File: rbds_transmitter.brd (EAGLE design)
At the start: 80 x 75.9 mm, 136 parts, among them J2 AVRISP-6, Q1 P-CH, Q2 P-Ch, Q3 P-Ch, T1 ATB3225-75032CT, T2 ATB3225-75032CT, U1 MAX2606, U2 TS974, U3 TS974, U4 MAX1551, U5 ATMEGA328, U6 TPS61030, U7 MCP4812, X1 16Mhz

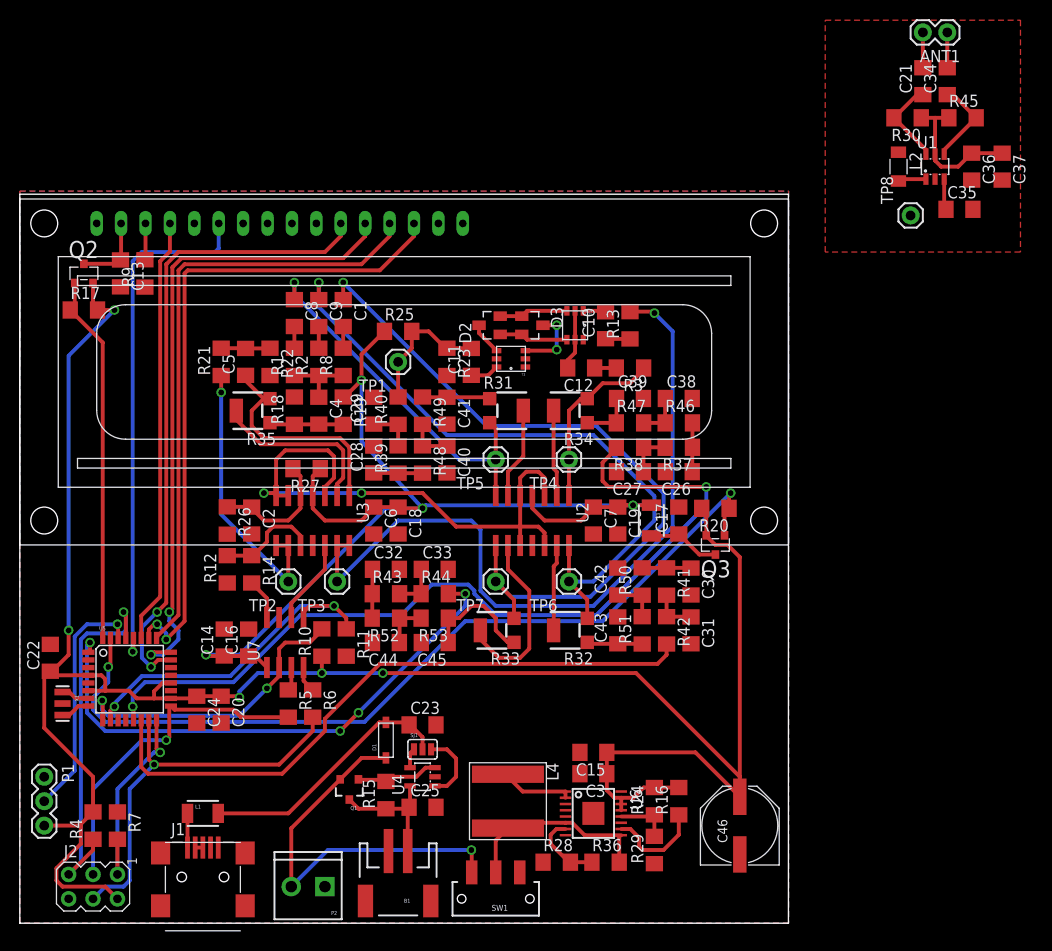
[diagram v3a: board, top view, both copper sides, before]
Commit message: renubmered everything, request engineering change forum
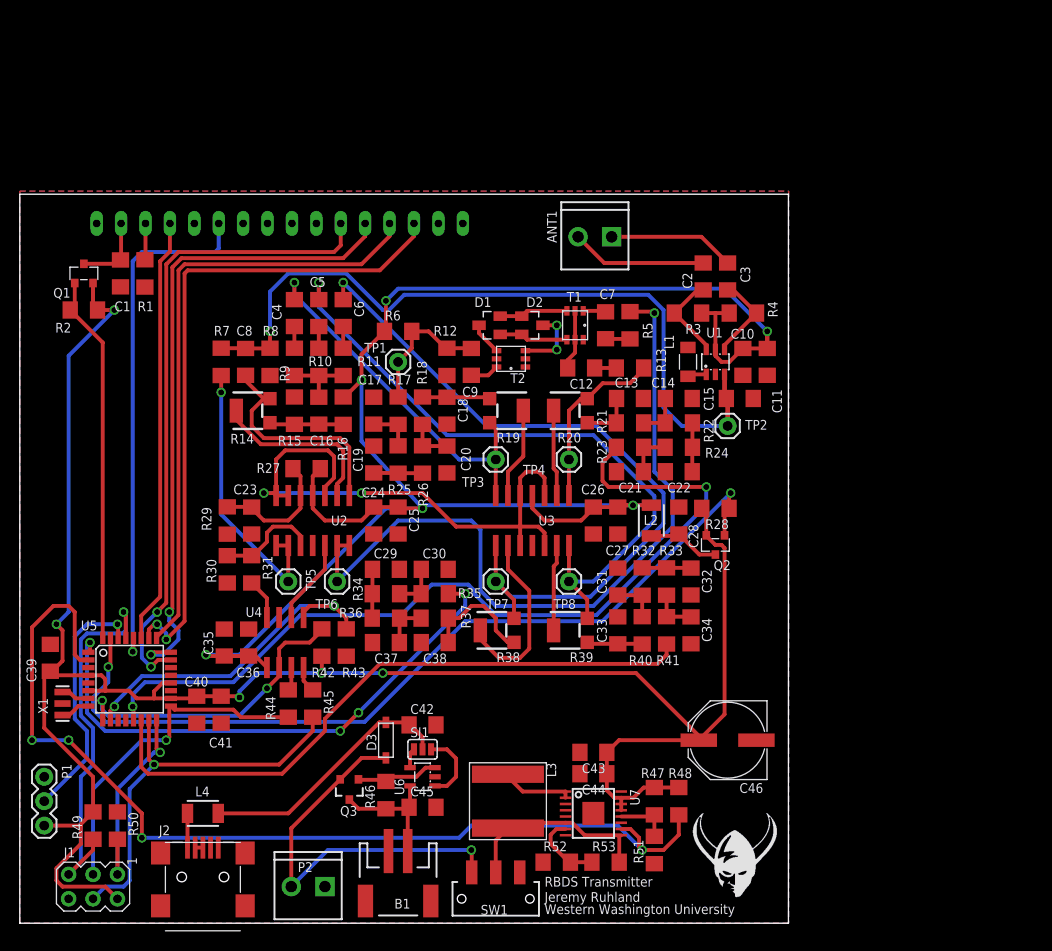
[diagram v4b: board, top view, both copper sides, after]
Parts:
- ANT1: value (none) -> 2.5MM; device dipole_antenna:ANT -> dipole_antenna:2.5MM_SCREW
- C1: value 1uF -> 4.7uF
- C10: value 10uF -> 1uF
- C11: value 10uF -> 4.7uF
- C13, C14: value 4.7uF -> 1.5nF
- C15: value 4.7uF -> 1nF
- C16, C24: value 0.1uF -> 1uF
- C17, C18, C19, C20: value 4.7uF -> 1.2nF
- C2, C3: value 1uF -> 1nF
- C21: value 1nF -> 1.5nF
- C22: value 0.1uF -> 1.5nF
- C23: value 4.7uF -> 1uF
- C26: value 1.5nF -> 1uF
- C27: value 1.5nF -> 4.7uF
- C28, C41: value 1.2nF -> 4.7uF
- C29: value 1.2nF -> 3nF
- C30: value 3.9nF -> 3nF
- C32, C33: value 3nF -> 3.9nF
- C34: value 1nF -> 3.9nF
- C35: value 1nF -> 4.7uF
- C36: value 1uF -> 0.1uF
- C37: value 4.7uF -> 3nF
- C38: value 1.5nF -> 3nF
- C39: value 1.5nF -> 0.1uF
- C40: value 1.2nF -> 0.1uF
- C42, C43: value 3.9nF -> 4.7uF
- C44: value 3nF -> 1uF
- C45: value 3nF -> 4.7uF
- C7, C9: value 1uF -> 10uF
- D1: value (none) -> BAS40-04; device adafruit:SOD-123 -> diode:SOT23
- D3: value BAS40-04 -> (none); device diode:SOT23 -> adafruit:SOD-123
- J1: value (none) -> AVRISP-6; device adafruit:USB-MINIB -> adafruit:AVRISP
- J2: value AVRISP-6 -> (none); device adafruit:AVRISP -> adafruit:USB-MINIB
- L1: value (none) -> 485nH; device sparkfun:1210 -> resistor:L3216C
- L2: value 485nH -> 10mH; device resistor:L3216C -> sparkfun:1210
- L3: value 10mH -> 6.8uH; device sparkfun:1210 -> yuden:8040
- L4: value 6.8uH -> (none); device yuden:8040 -> sparkfun:1210
- LCD1: value HD44780LCD-1602 -> HD44780LCDNOSILK; device adafruit:LCD1602 -> adafruit:LCD1602_NOSILK
- Q1: value P-CH -> P-Ch; device sparkfun:SOT23-3 -> transistor-power:MICRO3
- Q3: value P-Ch -> P-CH; device transistor-power:MICRO3 -> sparkfun:SOT23-3
- R1: value 1k -> 332
- R10, R11: value 10k -> 1k
- R12, R6, R7: value 10k -> 100k
- R14: value 10k -> 100k; device adafruit:R1206 -> rcl:RTRIM3304W
- R17, R18, R21, R22, R23, R25, R26: value 100k -> 2k
- R19, R20: device adafruit:R1206 -> rcl:RTRIM3304W
- R2, R8: value 1k -> 100k
- R24: value 1.8M -> 2k
- R28: value 390k -> 100k
- R29: value 200k -> 100k
- R3: value 200 -> 100
- R30, R45: value 100 -> 10k
- R31: value 100k -> 10k; device rcl:RTRIM3304W -> adafruit:R1206
- R32, R33, R34, R35: value 100k -> 2k; device rcl:RTRIM3304W -> adafruit:R1206
- R36: value 1.95M -> 2k
- R38, R39: value 2k -> 100k; device adafruit:R1206 -> rcl:RTRIM3304W
- R4: value 10k -> 100
- R42, R43, R44, R49, R50: value 2k -> 10k
- R46, R48: value 2k -> 100k
- R47: value 2k -> 1.8M
- R5: value 10k -> 200
- R51: value 2k -> 200k
- R52: value 2k -> 390k
- R53: value 2k -> 1.95M
- R9: value 332 -> 1k
- U4: value MAX1551 -> MCP4812; device maxim:SOT23-5L -> microchip:SO-08
- U6: value TPS61030 -> MAX1551; device texas:HTSSOP16 -> maxim:SOT23-5L
- U7: value MCP4812 -> TPS61030; device microchip:SO-08 -> texas:HTSSOP16
- moved R45 91.0 mm to (30.5, 22.9), turned to 270 degrees
- moved C36 90.1 mm to (23.8, 29.2), turned to 90 degrees
- moved C35 88.8 mm to (21.3, 29.2), turned to 90 degrees
- moved R4 86.1 mm to (75.2, 63.5), turned to 0 degrees
- moved R30 85.0 mm to (21.6, 36.8), turned to 90 degrees
- moved C37 81.0 mm to (38.1, 29.2), turned to 180 degrees
- moved Q2 71.5 mm to (72.4, 39.4), turned to 180 degrees
- moved L1 69.0 mm to (69.5, 58.4), turned to 270 degrees
- moved C22 68.2 mm to (68.6, 47.0), turned to 180 degrees
- moved C39 66.1 mm to (3.17, 27.6), turned to 90 degrees
- moved C34 63.1 mm to (69.8, 30.5), turned to 270 degrees
- moved Q1 60.4 mm to (6.67, 67.6), turned to 0 degrees
- moved R50 60.2 mm to (10.2, 10.2), turned to 270 degrees
- moved R29 56.1 mm to (21.6, 41.9), turned to 270 degrees
- moved R49 55.1 mm to (7.62, 10.2), turned to 90 degrees
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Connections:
- net !DAC_CS: now also R42.2, U4.2; no longer R10.2, U7.2
- net !DAC_LATCH: now also R43.1, U4.5; no longer R11.1, U7.5
- net !ISP-RST: now also J1.5, R49.1; no longer J2.5, R4.1
- net !LCD_EN: now also Q1.1, R2.1; no longer Q2.1, R17.1
- net !TX_EN: now also Q2.1, R28.1; no longer Q3.1, R20.1
- net +5V: now also C39.1, C40.1, C41.1, C43.1, C44.1, J1.2, Q1.2, R2.2, R28.2, R42.1, R47.2, R48.2, R49.2, U7.13, U7.14, U7.15; no longer C15.1, C20.1, C22.1, C24.1, C3.1, J2.2, Q3.2, R10.1, R16.2, R17.2, R20.2, R24.2, R4.2, U6.13, U6.14, U6.15
- net AGND: now also U2.6, U2.7, U3.10, U3.12, U3.5; no longer U2.10, U2.12, U2.5, U3.6, U3.7
- net BPSK: now also R5.2, TP6.1, U2.13, U2.14; no longer R13.2, TP3.1, U3.13, U3.14
- net CARRIER: now also R23.2; no longer R38.2
- net FREQUENCY: now also R7.1, TP5.1, U2.8, U2.9; no longer R21.1, TP2.1, U3.8, U3.9
- net GND: now also C1.2, C10.2, C11.2, C21.2, C34.2, J1.6, J2.GND, L1.1, R1.1, R12.2, R15.2, R29.2, R30.1, R43.2, R51.1, R52.1, R8.2, U4.7, U6.2, U7.11, U7.3, U7.4, U7.5, U7.8, U7.EXP; no longer C16.2, C2.2, C3.2, C6.2, C7.2, J1.GND, J2.6, L2.1, R11.2, R12.1, R18.2, R22.2, R23.2, R26.2, R28.1, R29.1, R9.1, U4.2, U6.11, U6.3, U6.4, U6.5, U6.8, U6.EXP, U7.7
- net ISP-MISO: now also J1.1, R50.2; no longer J2.1, R7.2
- net ISP-MOSI: now also J1.4, R45.2; no longer J2.4, R6.2
- net ISP-SCK: now also J1.3, R44.2; no longer J2.3, R5.2
- net LOWBAT: now also R48.1, U7.10; no longer R16.1, U6.10
- net MISO: now also R50.1; no longer R7.1
- net MOSI: now also R45.1, U4.4; no longer R6.1, U7.4
- net N$1: now also C42.1, D3.A, L4.2; no longer C23.1, D1.A, L1.2
- net N$10: now also Q3.1, R46.2, U6.3; no longer Q1.1, R15.2, U4.3
- net N$11: now also C45.1, Q3.3, R46.1, U6.5; no longer C25.1, Q1.3, R15.1, U4.5
- net N$12: now also L3.1, U7.1, U7.2; no longer L4.1, U6.1, U6.2
- net N$13: now also J2.D+, J2.D-; no longer J1.D+, J1.D-
- net N$14: now also D2.3; no longer D3.3
- net N$15: now also D3.C, Q3.2; no longer D1.C, Q1.2
- net N$16: now also D1.2, D2.1; no longer D2.2, D3.1
- net N$17: now also R47.1, R51.2, U7.12; no longer R24.1, R29.2, U6.12
- net N$18: now also D1.1, D2.2; no longer D2.1, D3.2
- net N$20: now also C7.2; no longer C10.2
- net N$21: now also C28.1, L2.2, Q2.3; no longer C17.1, L3.2, Q3.3
- net N$22: now also R14.2, U2.2; no longer R35.2, U3.2
- net N$23: now also C8.1, R14.3, U2.1; no longer C5.1, R35.3, U3.1
- net N$24: now also L1.2; no longer L2.2
- net N$25: now also C7.1, R5.1; no longer C10.1, R13.1
- net N$26: now also R13.2; no longer R3.2
- net N$27: now also R31.2, U4.8; no longer R14.2, U7.8
- net N$28: now also U2.12, U4.6; no longer U3.12, U7.6
- net N$3: now also D1.3; no longer D2.3
- net N$33: now also C2.1, R3.2; no longer C21.1, R30.2
- net N$35: now also C3.1, R4.2; no longer C34.1, R45.2
- net N$39: now also C2.2; no longer C21.2
- net N$42: now also C9.1; no longer C11.1
- net N$46: now also R30.2, R31.1, U2.10; no longer R12.2, R14.1, U3.10
- net N$5: now also C16.2, R14.1, R15.1, R16.2; no longer C4.2, R18.1, R19.2, R35.1
- net N$50: now also L3.2, R53.2, U7.6, U7.9; no longer L4.2, R36.2, U6.6, U6.9
- net N$52: now also C3.2; no longer C34.2
- net N$54: now also J2.VBUS, L4.1; no longer J1.VBUS, L1.1
- net N$55: now also C21.1, R23.1, R24.2; no longer C27.1, R37.2, R38.1
- net N$59: now also C22.1, R22.2, R24.1; no longer C26.1, R37.1, R46.2
- net N$60: now also C19.1, R25.1, R26.2; no longer C28.1, R39.1, R48.2
- net N$61: now also C20.1, R18.2, R26.1; no longer C40.1, R48.1, R49.2
- net N$62: now also C18.1, R18.1, R19.1; no longer C41.1, R31.1, R49.1
- net N$63: now also C13.1, R20.1, R21.1; no longer C39.1, R34.1, R47.1
- net N$64: now also R19.2, U3.6; no longer R31.2, U2.6
- net N$65: now also C4.1, R19.3, TP3.1, U3.7; no longer C8.1, R31.3, TP5.1, U2.7
- net N$66: now also C23.1, R29.1, U2.5; no longer C2.1, R26.1, U3.5
- net N$67: now also C32.1, R32.2, R33.1; no longer C30.1, R41.1, R50.2
- net N$68: now also C31.1, R32.1, R40.2; no longer C42.1, R50.1, R51.2
- net N$69: now also C33.1, R39.1, R40.1; no longer C43.1, R32.1, R51.1
- net N$7: now also U6.1; no longer U4.1
- net N$70: now also R39.2, U3.13; no longer R32.2, U2.13
- net N$71: now also C5.1, R39.3, TP8.1, U3.14; no longer C9.1, R32.3, TP6.1, U2.14
- net N$72: now also C29.1, R34.1, R36.2; no longer C32.1, R43.1, R52.2
- net N$73: now also C37.1, R36.1, R37.2; no longer C44.1, R52.1, R53.2
- net N$74: now also C38.1, R37.1, R38.1; no longer C45.1, R33.1, R53.1
- net N$75: now also R38.2, U3.9; no longer R33.2, U2.9
- net N$76: now also C6.1, R38.3, U3.8; no longer C1.1, R33.3, U2.8
- net N$77: now also R20.2, U3.2; no longer R34.2, U2.2
- net N$78: now also C4.2, R9.2; no longer C8.2, R1.2
- net N$79: now also C5.2, R10.2; no longer C9.2, R2.2
- net N$8: now also U6.4; no longer U4.4
- net N$80: now also C6.2, R11.2; no longer C1.2, R8.2
- net N$81: now also C16.1, R10.1, R11.1, R9.1; no longer C4.1, R1.1, R2.1, R8.1
- net N$82: now also R13.1, R20.3, U3.1; no longer R3.1, R34.3, U2.1
- net N$83: now also C17.1, R17.1, R25.2; no longer C29.1, R39.2, R40.1
- net N$84: now also C34.1, R33.2, R41.1; no longer C31.1, R41.2, R42.1
- net N$85: now also C30.1, R34.2, R35.1; no longer C33.1, R43.2, R44.1
- net N$86: now also C14.1, R21.2, R22.1; no longer C38.1, R46.1, R47.2
- net N$9: now also R1.2; no longer R9.2
- net PILOT: now also R41.2; no longer R42.2
- net RBDS: now also C9.2, R12.1, R17.2, R6.2; no longer C11.2, R23.1, R25.2, R40.2
- net SCK: now also R44.1, U4.3; no longer R5.1, U7.3
- net SIGNAL: now also C15.1, C8.2, R7.2, R8.1, TP2.1; no longer C35.1, C5.2, R21.2, R22.1, TP8.1
- net TONE: now also R35.2; no longer R44.2
- net U7: now also R52.2, R53.1, U7.7; no longer R28.2, R36.1, U6.7
- net VCC: now also C10.1, C11.1, C24.1, C25.1, C26.1, C27.1, C35.1, L2.1, R16.1, R3.1, R4.1, R6.1, U4.1; no longer C14.1, C16.1, C18.1, C19.1, C37.1, C6.1, C7.1, L3.1, R19.1, R25.1, R30.1, R45.1, U7.1
- net VDD: now also C1.1, Q1.3; no longer C13.1, Q2.3
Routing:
- net LOWBAT: track 10.2 -> 104.6 mm, vias 0 -> 4
- net SIGNAL: track 8.32 -> 84.2 mm, vias 0 -> 1
- net VCC: track 134.4 -> 182.5 mm, vias 4 -> 6
- net +5V: track 232.7 -> 216.2 mm
- net N$39: track 3.68 -> 14.2 mm
- net N$52: track 3.68 -> 13.2 mm
- net N$24: track 3.10 -> 1.99 mm
- net RXD: track 24.9 -> 25.9 mm
- net !ISP-RST: track 39.6 -> 40.6 mm
- net LCD2: track 66.4 -> 67.0 mm
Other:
- board text added: "Jeremy Ruhland"
- board text added: "RBDS Transmitter"
- board text added: "Western Washington University"
